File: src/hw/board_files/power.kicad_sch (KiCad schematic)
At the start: 23 parts, among them P2 USB_C_Plug_USB2.0, SW1 SW_SPDT, U3 TPS63031DSKR, U5 MCP73831T-2ACI/OT

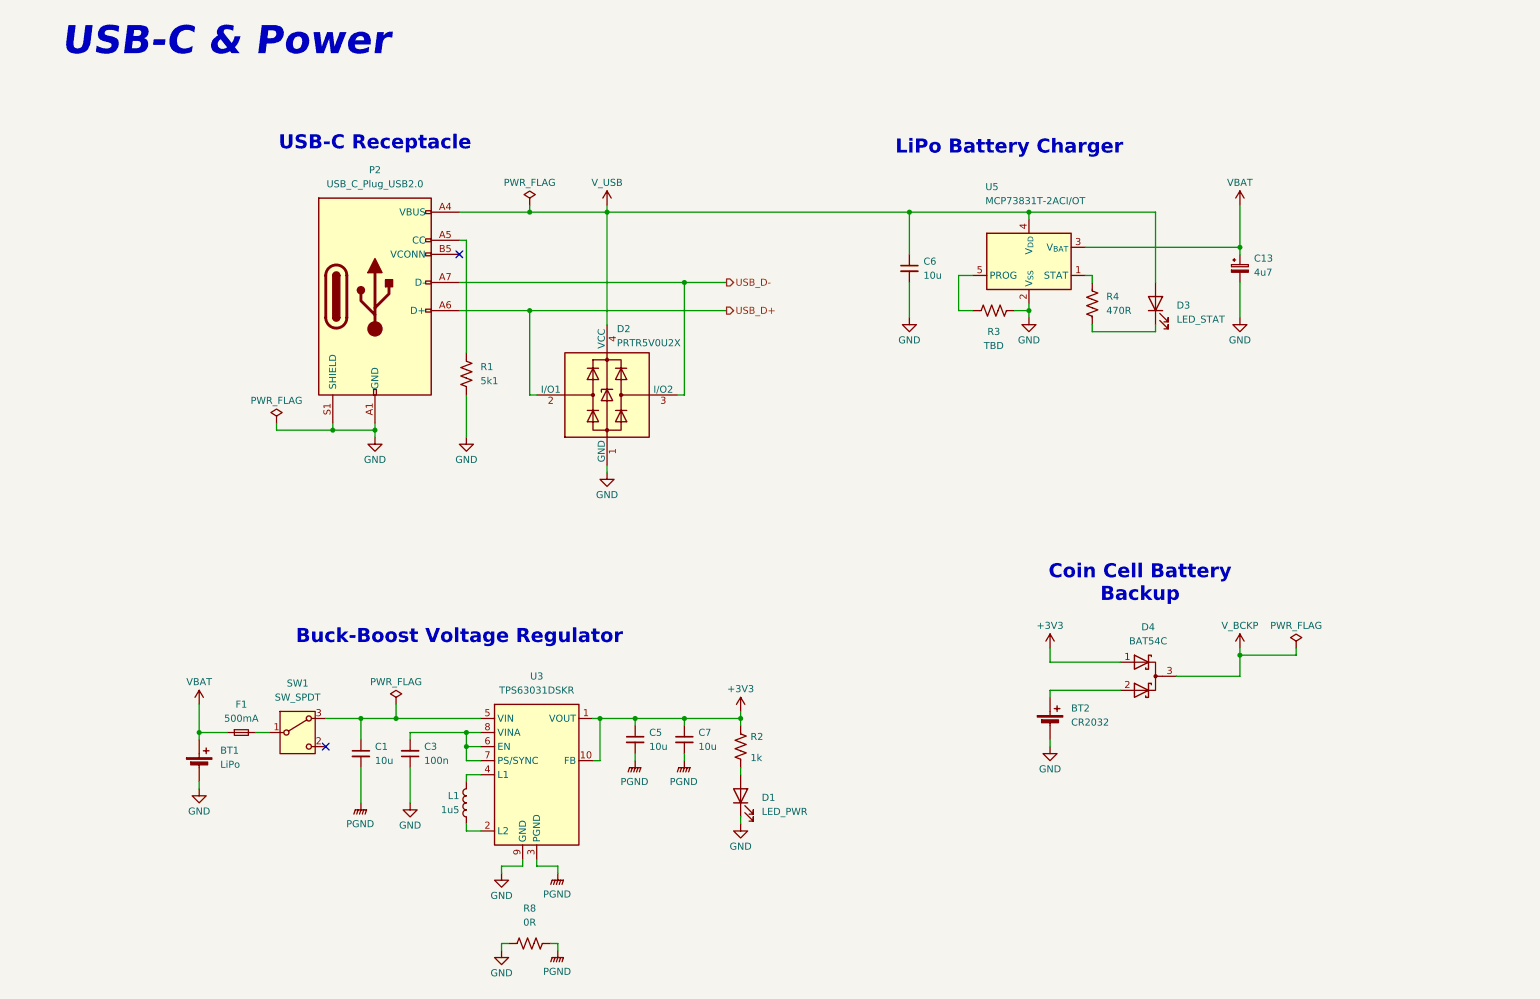
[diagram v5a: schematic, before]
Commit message: Put USB to UART bridge back and added jumpers to USB lines
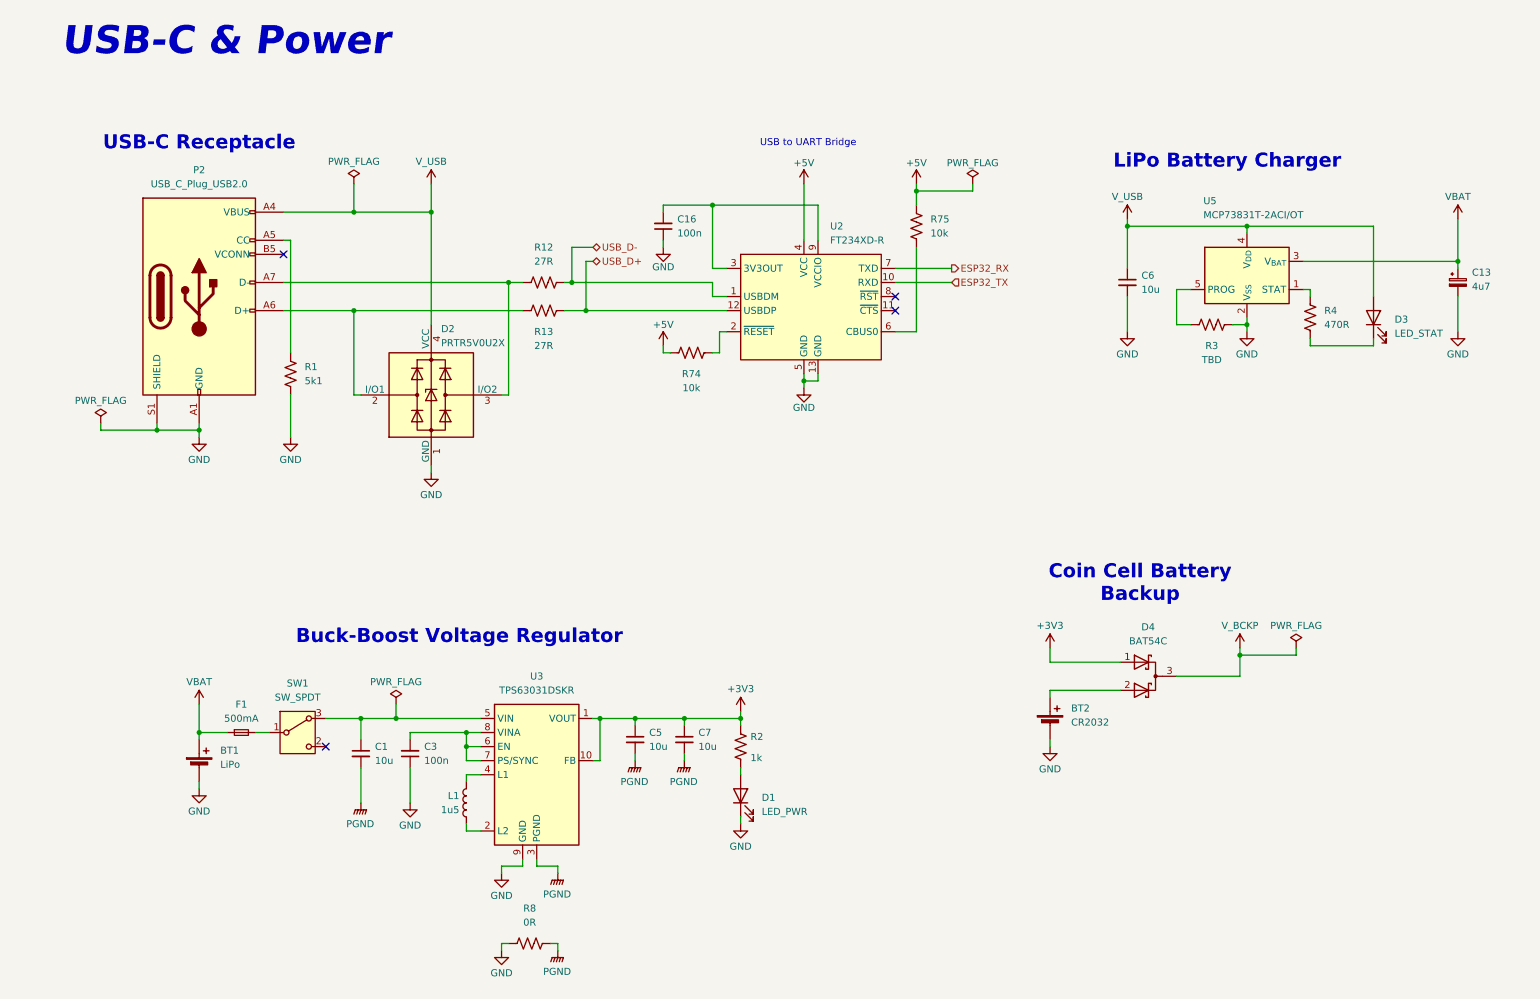
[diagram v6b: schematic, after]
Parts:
- added C16: 100n, Capacitor_SMD:C_0603_1608Metric, symbol Device:C_Small
- added R12, R13: 27R, Resistor_SMD:R_0603_1608Metric, symbol Device:R_US
- added R74, R75: 10k, Resistor_SMD:R_0603_1608Metric, symbol Device:R_US
- added U2: FT234XD-R, Package_DFN_QFN:DFN-12-1EP_3x3mm_P0.45mm_EP1.65x2.38mm, symbol smart_clock:FT234XD-R
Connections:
- net GND: now also C16.1, U2.13 (GND), U2.5 (GND)
- net USB_D+: now also R13.1, U2.12 (USBDP); no longer D2.2 (I/O1), P2.A6 (D+)
- net USB_D-: now also R12.1, U2.1 (USBDM); no longer D2.3 (I/O2), P2.A7 (D-)
- new net: D2.3 (I/O2), P2.A7 (D-), R12.2
- new net: R74.1, U2.2 (~{RESET})
- new net: C16.2, U2.3 (3V3OUT), U2.9 (VCCIO)
- new net: R75.2, U2.6 (CBUS0)
- new net: D2.2 (I/O1), P2.A6 (D+), R13.2
- new net +5V: R74.2, R75.1, U2.4 (VCC)
- new net ESP32_RX: U2.7 (TXD)
- new net ESP32_TX: U2.10 (RXD)
- no-connect marks 2 -> 4
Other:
- note added: "USB to UART Bridge"
- moved on the sheet: C13, C6, D2, D3, P2, R1, R3, R4, U5

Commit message: Added fuel gauge if, push buttons, jumpers. Need to add test points then review schematic.
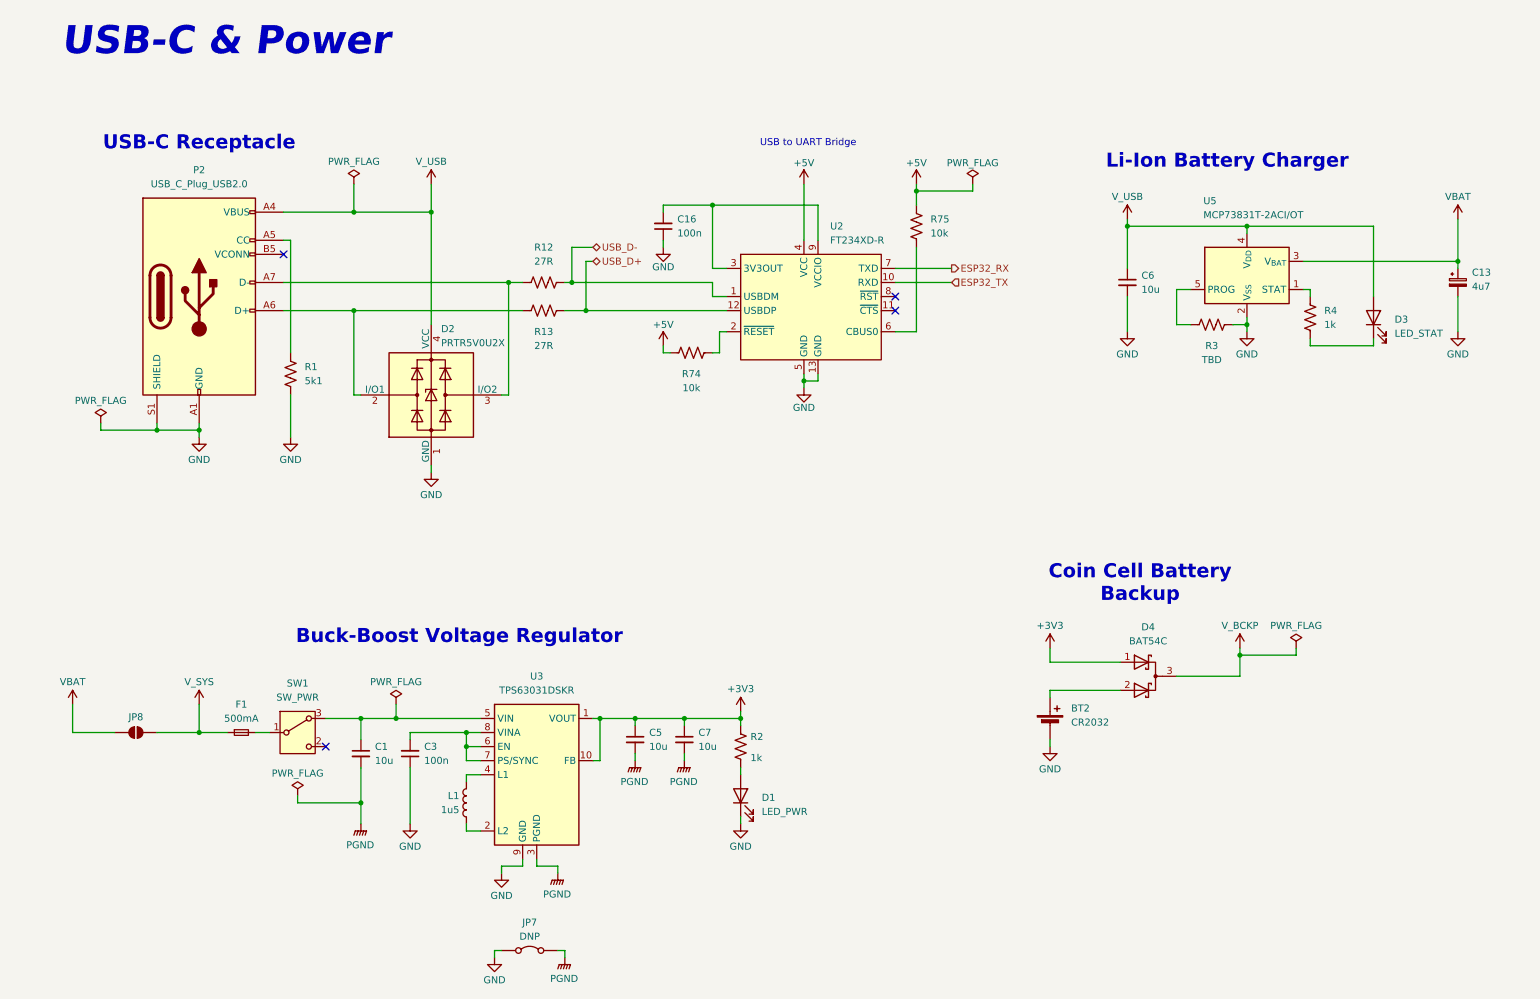
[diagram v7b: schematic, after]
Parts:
- removed BT1: LiPo, Connector_JST:JST_PH_S2B-PH-K_1x02_P2.00mm_Horizontal, symbol Device:Battery_Cell
- removed R8: 0R, symbol Device:R_US
- added JP7: DNP, symbol Jumper:Jumper_2_Bridged
- added JP8: SolderJumper_Open, symbol Jumper:SolderJumper_2_Open
- R4: value 470R -> 1k
- SW1: value SW_SPDT -> SW_PWR
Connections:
- net GND: now also JP7.1 (A)
- net PGND: now also JP7.2 (B)
- net VBAT: now also JP8.1 (A); no longer F1.1
- new net V_SYS: F1.1, JP8.2 (B)
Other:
- note added: "Li-Ion Battery Charger"
- note removed: "LiPo Battery Charger"

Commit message: Added Test Points to Schematic
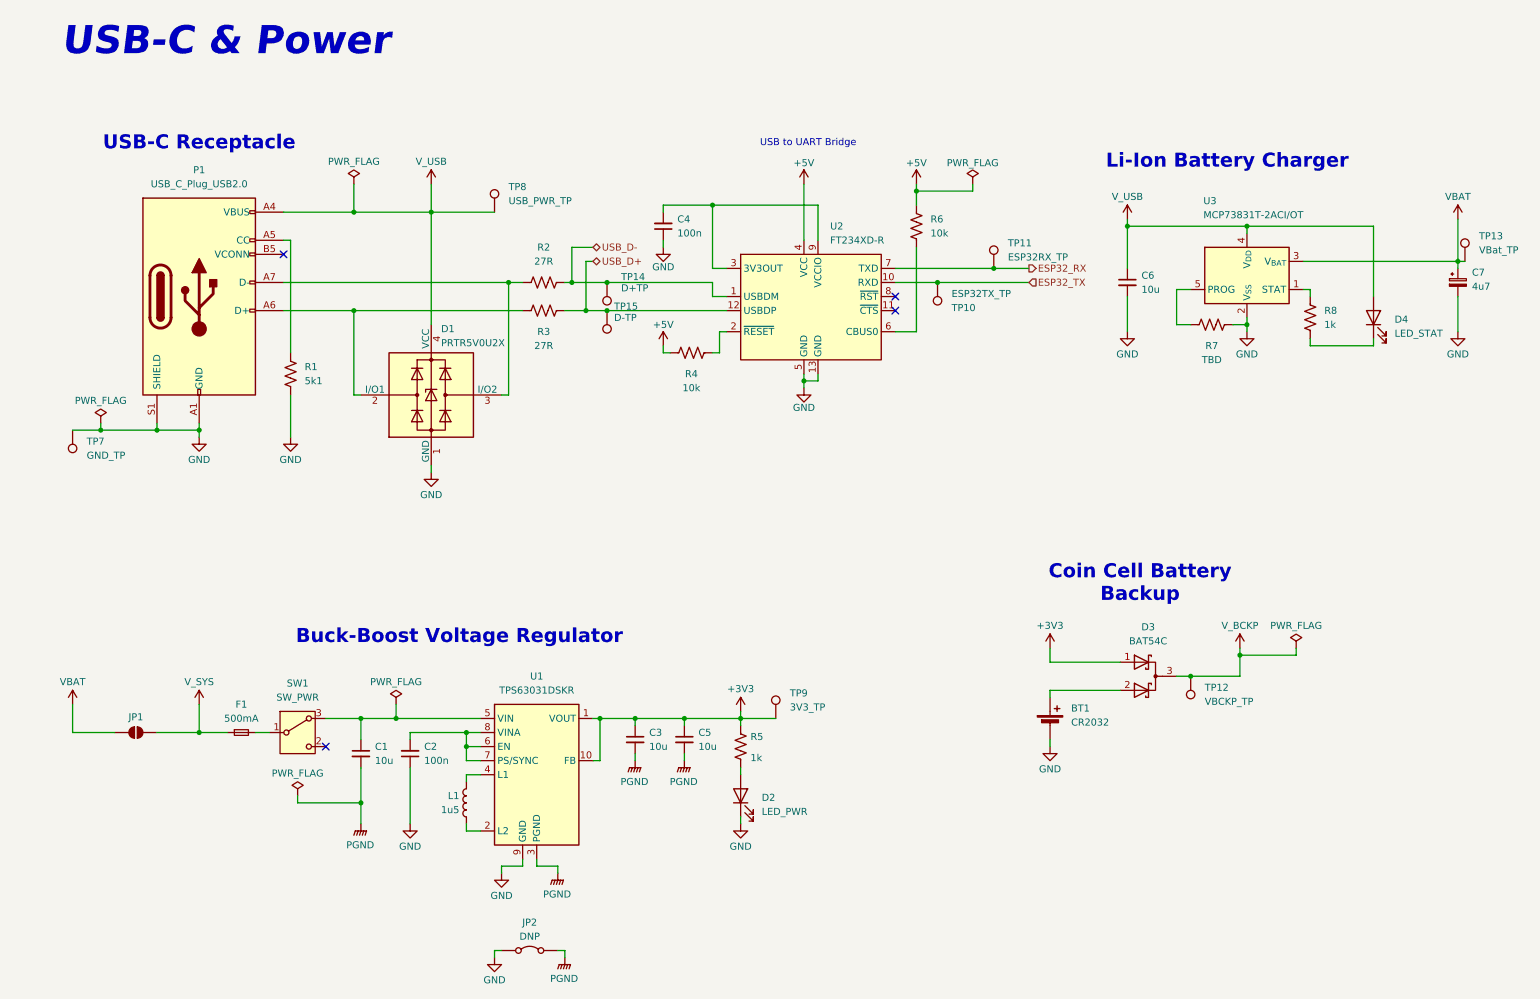
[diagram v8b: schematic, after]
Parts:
- added TP10: ESP32TX_TP, symbol Connector:TestPoint
- added TP11: ESP32RX_TP, symbol Connector:TestPoint
- added TP12: VBCKP_TP, symbol Connector:TestPoint
- added TP13: VBat_TP, symbol Connector:TestPoint
- added TP14: D+TP, symbol Connector:TestPoint
- added TP15: D-TP, symbol Connector:TestPoint
- added TP7: GND_TP, symbol Connector:TestPoint
- added TP8: USB_PWR_TP, symbol Connector:TestPoint
- added TP9: 3V3_TP, symbol Connector:TestPoint
- renumbered BT2 to BT1, C3 to C2, C5 to C3, C16 to C4, C7 to C5, C13 to C7, D2 to D1, D1 to D2, D4 to D3, D3 to D4, JP8 to JP1, JP7 to JP2, P2 to P1, R12 to R2, R13 to R3, R74 to R4, R2 to R5, R75 to R6, R3 to R7, R4 to R8, U3 to U1, U5 to U3
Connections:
- net +3V3: now also TP9.1
- net ESP32_RX: now also TP11.1
- net ESP32_TX: now also TP10.1
- net GND: now also TP7.1
- net USB_D+: now also TP15.1
- net USB_D-: now also TP14.1
- net VBAT: now also TP13.1
- net V_BCKP: now also TP12.1
- net V_USB: now also TP8.1
